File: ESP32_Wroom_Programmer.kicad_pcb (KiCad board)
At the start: 2 copper layers, 40.6 x 18 mm, 20 parts, among them J1 USB_C_Receptacle_USB2.0_16P, Q1 SS8050, Q2 SS8050, U1 Torex Semicon XC6206P332MR-G, U2 CH340C

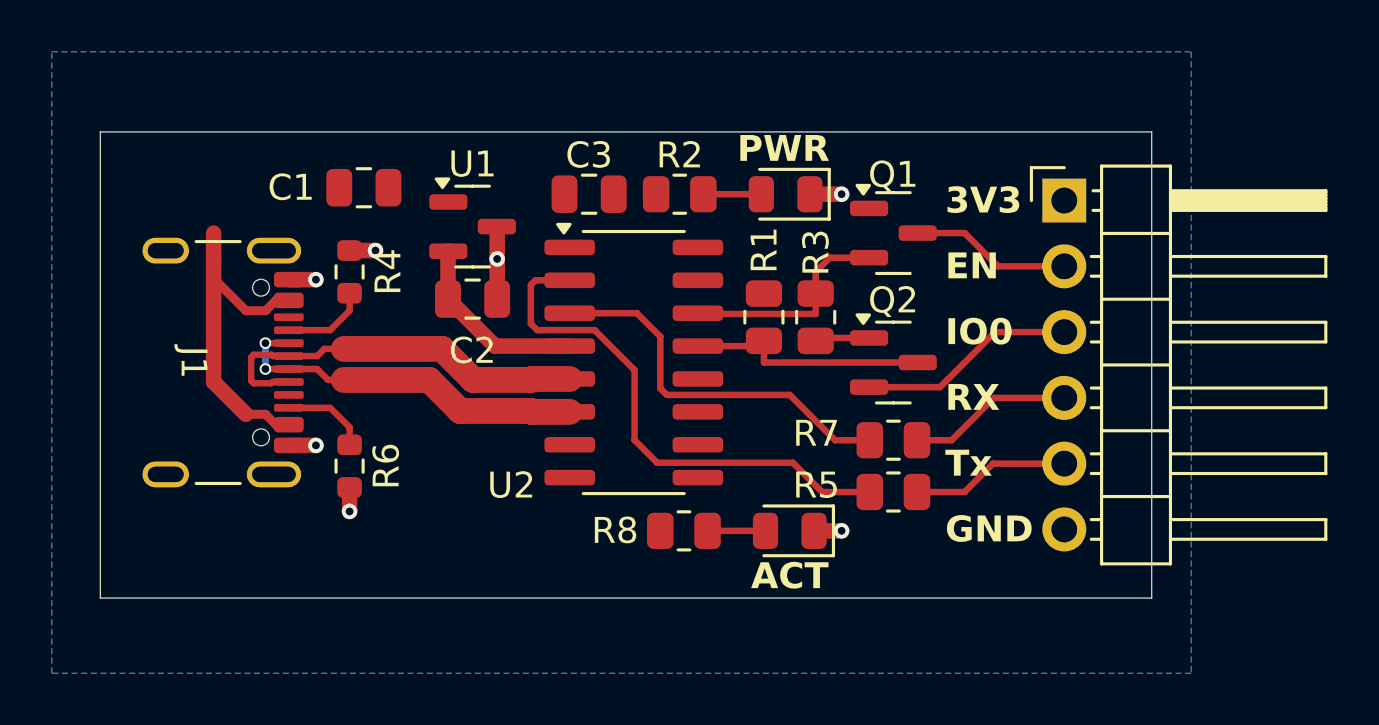
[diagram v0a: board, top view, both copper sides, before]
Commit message: fixed missing +3V3 connections
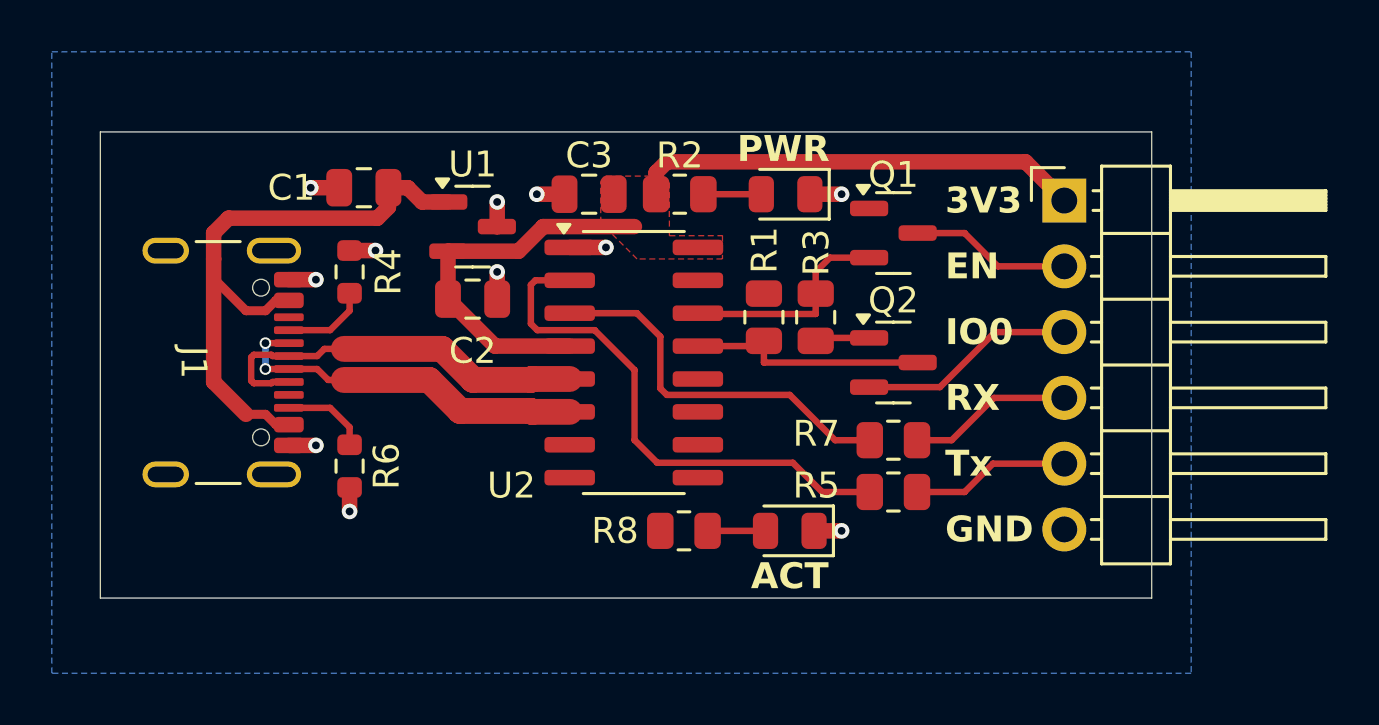
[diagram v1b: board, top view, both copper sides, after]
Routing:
- net +3V3: track 7.50 -> 32.5 mm
- net VBUS: track 13.7 -> 24.1 mm
- net GND: track 9.12 -> 11.7 mm, vias 7 -> 11
- added copper zone on F.Cu, net +3V3
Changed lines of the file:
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@@
 		(tags "capacitor")
 		(property "Reference" "C2"
-			(at 0 2.000001 360)
+			(at 0 2.000001 0)
 			(layer "F.SilkS")
 			(effects
@@
 		)
 		(property "Value" "1u"
-			(at 0 1.679999 360)
+			(at 0 1.679999 0)
 			(layer "F.Fab")
 			(effects
@@
 		)
 		(fp_text user "${REFERENCE}"
-			(at 0 0 360)
+			(at 0 0 0)
 			(layer "F.Fab")
 			(effects
@@
 		(tags "SOT TO_SOT_SMD")
 		(property "Reference" "U1"
-			(at 0 -2.4 360)
+			(at 0 -2.4 0)
 			(layer "F.SilkS")
 			(effects
@@
 		)
 		(property "Value" "Torex Semicon XC6206P332MR-G"
-			(at 0 2.4 360)
+			(at 0 2.4 0)
 			(layer "F.Fab")
 			(effects
@@
 		)
 		(fp_text user "${REFERENCE}"
-			(at 0 0 360)
+			(at 0 0 0)
 			(layer "F.Fab")
 			(effects
@@
 		(tags "capacitor")
 		(property "Reference" "C1"
-			(at 2.800001 0 360)
+			(at 2.800001 0 0)
 			(layer "F.SilkS")
 			(effects
@@
 		)
 		(property "Value" "1u"
-			(at 0 1.679999 360)
+			(at 0 1.679999 0)
 			(layer "F.Fab")
 			(effects
@@
 		)
 		(fp_text user "${REFERENCE}"
-			(at 0 0 360)
+			(at 0 0 0)
 			(layer "F.Fab")
 			(effects
@@
 	)
 	(segment
-		(start 142.199999 96)
-		(end 142.199999 94.762498)
+		(start 136.5 95.675)
+		(end 137.5 95.675)
 		(width 0.6)
 		(layer "F.Cu")
@@
 	)
 	(segment
-		(start 136.5 95.675)
-		(end 137.5 95.675)
+		(start 142.2 97.549999)
+		(end 142.199999 97.55)
 		(width 0.6)
 		(layer "F.Cu")
@@
 	)
 	(segment
-		(start 136.5 104.85)
-		(end 136.475 104.825)
+		(start 145 95.555)
+		(end 146.4 95.555)
+		(width 0.6)
+		(layer "F.Cu")
+		(net 1)
+	)
+	(segment
+		(start 142.2 94.737501)
+		(end 142.187501 94.75)
 		(width 0.6)
 		(layer "F.Cu")
@@
 	)
 	(segment
-		(start 142.199999 97.55)
-		(end 142.199999 96)
+		(start 143.731249 93.5)
+		(end 144.66875 93.5)
+		(width 0.6)
+		(layer "F.Cu")
+		(net 1)
+	)
+	(segment
+		(start 135.999999 93.25)
+		(end 135.000001 93.25)
+		(width 0.6)
+		(layer "F.Cu")
+		(net 1)
+	)
+	(segment
+		(start 142.2 96.5)
+		(end 142.2 97.549999)
+		(width 0.6)
+		(layer "F.Cu")
+		(net 1)
+	)
+	(segment
+		(start 136.5 104.85)
+		(end 136.475 104.825)
 		(width 0.6)
 		(layer "F.Cu")
@@
 		(net 1)
 	)
+	(segment
+		(start 142.2 93.8)
+		(end 142.2 94.737501)
+		(width 0.6)
+		(layer "F.Cu")
+		(net 1)
+	)
 	(via
 		(at 137.5 95.675)
@@
 	)
 	(via
+		(at 135.000001 93.25)
+		(size 0.6)
+		(drill 0.3)
+		(layers "F.Cu" "B.Cu")
+		(free yes)
+		(net 1)
+	)
+	(via
+		(at 143.731249 93.5)
+		(size 0.6)
+		(drill 0.3)
+		(layers "F.Cu" "B.Cu")
+		(free yes)
+		(net 1)
+	)
+	(via
 		(at 155.5 93.5)
 		(size 0.6)
@@
 	)
 	(via
+		(at 142.2 93.8)
+		(size 0.6)
+		(drill 0.3)
+		(layers "F.Cu" "B.Cu")
+		(free yes)
+		(net 1)
+	)
+	(via
 		(at 135.2 96.8)
 		(size 0.6)
@@
 	)
 	(via
-		(at 142.199999 96)
+		(at 146.4 95.555)
 		(size 0.6)
 		(drill 0.3)
 		(layers "F.Cu" "B.Cu")
+		(free yes)
+		(net 1)
+	)
+	(via
+		(at 142.2 96.5)
+		(size 0.6)
+		(drill 0.3)
+		(layers "F.Cu" "B.Cu")
+		(free yes)
 		(net 1)
 	)
@@
 	)
 	(segment
+		(start 131.25 95)
+		(end 131.825 94.425)
+		(width 0.6)
+		(layer "F.Cu")
+		(net 3)
+	)
+	(segment
+		(start 140.3125 93.8)
+		(end 139.3 93.8)
+		(width 0.6)
+		(layer "F.Cu")
+		(net 3)
+	)
+	(segment
 		(start 133.656317 102.4)
 		(end 133.256317 102)
@@
 	)
 	(segment
+		(start 138 94)
+		(end 138 93.25)
+		(width 0.6)
+		(layer "F.Cu")
+		(net 3)
+	)
+	(segment
 		(start 133.656317 97.6)
 		(end 133.256317 98)
@@
 	)
 	(segment
+		(start 139.3 93.8)
+		(end 138.75 93.25)
+		(width 0.6)
+		(layer "F.Cu")
+		(net 3)
+	)
+	(segment
 		(start 132.5 98)
 		(end 131.25 96.75)
@@
 	)
 	(segment
+		(start 138.75 93.25)
+		(end 138 93.25)
+		(width 0.6)
+		(layer "F.Cu")
+		(net 3)
+	)
+	(segment
 		(start 133.256317 98)
 		(end 132.5 98)
@@
 	)
 	(segment
-		(start 131.25 95)
-		(end 131.25 96)
+		(start 137.575 94.425)
+		(end 138 94)
+		(width 0.6)
+		(layer "F.Cu")
+		(net 3)
+	)
+	(segment
+		(start 131.25 96)
+		(end 131.25 95)
 		(width 0.6)
 		(layer "F.Cu")
@@
 	)
 	(segment
+		(start 131.825 94.425)
+		(end 137.575 94.425)
+		(width 0.6)
+		(layer "F.Cu")
+		(net 3)
+	)
+	(segment
 		(start 134.155 102.4)
 		(end 133.656317 102.4)
@@
 	)
 	(segment
+		(start 140.3125 95.7)
+		(end 143.027316 95.7)
+		(width 0.6)
+		(layer "F.Cu")
+		(net 4)
+	)
+	(segment
+		(start 148.75 92.25)
+		(end 148.3375 92.6625)
+		(width 0.6)
+		(layer "F.Cu")
+		(net 4)
+	)
+	(segment
 		(start 148.262499 93.575001)
 		(end 148.3375 93.5)
@@
 	)
 	(segment
+		(start 148.3375 92.6625)
+		(end 148.3375 93.5)
+		(width 0.6)
+		(layer "F.Cu")
+		(net 4)
+	)
+	(segment
 		(start 148.3375 93.5)
 		(end 148.425 93.5)
@@
 	)
 	(segment
+		(start 164.1 93.745)
+		(end 162.605 92.25)
+		(width 0.6)
+		(layer "F.Cu")
+		(net 4)
+	)
+	(segment
+		(start 162.605 92.25)
+		(end 148.75 92.25)
+		(width 0.6)
+		(layer "F.Cu")
+		(net 4)
+	)
+	(segment
+		(start 143.977316 94.75)
+		(end 147.5 94.75)
+		(width 0.6)
+		(layer "F.Cu")
+		(net 4)
+	)
+	(segment
+		(start 143.027316 95.7)
+		(end 143.977316 94.75)
+		(width 0.6)
+		(layer "F.Cu")
+		(net 4)
+	)
+	(segment
 		(start 140.300001 95.712499)
 		(end 140.3125 95.7)
@@
 	)
 	(zone
+		(net 4)
+		(net_name "+3V3")
+		(layer "F.Cu")
+		(hatch edge 0.5)
+		(priority 100)
+		(connect_pads yes
+			(clearance 0.2)
+		)
+		(min_thickness 0.2)
+		(filled_areas_thickness no)
+		(fill yes
+			(thermal_gap 0.2)
+			(thermal_bridge_width 0.5)
+		)
+		(polygon
+			(pts
+				(xy 146.2 93) (xy 146.4 92.8) (xy 148.6 92.8) (xy 148.847617 93.048547) (xy 148.847617 94.148547)
+				(xy 148.850514 95.103114) (xy 150.9 95.1) (xy 150.9 96) (xy 147.6 96) (xy 146.2 94.6)
+			)
+		)
+	)
+	(zone

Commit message: there were still some connections missing...
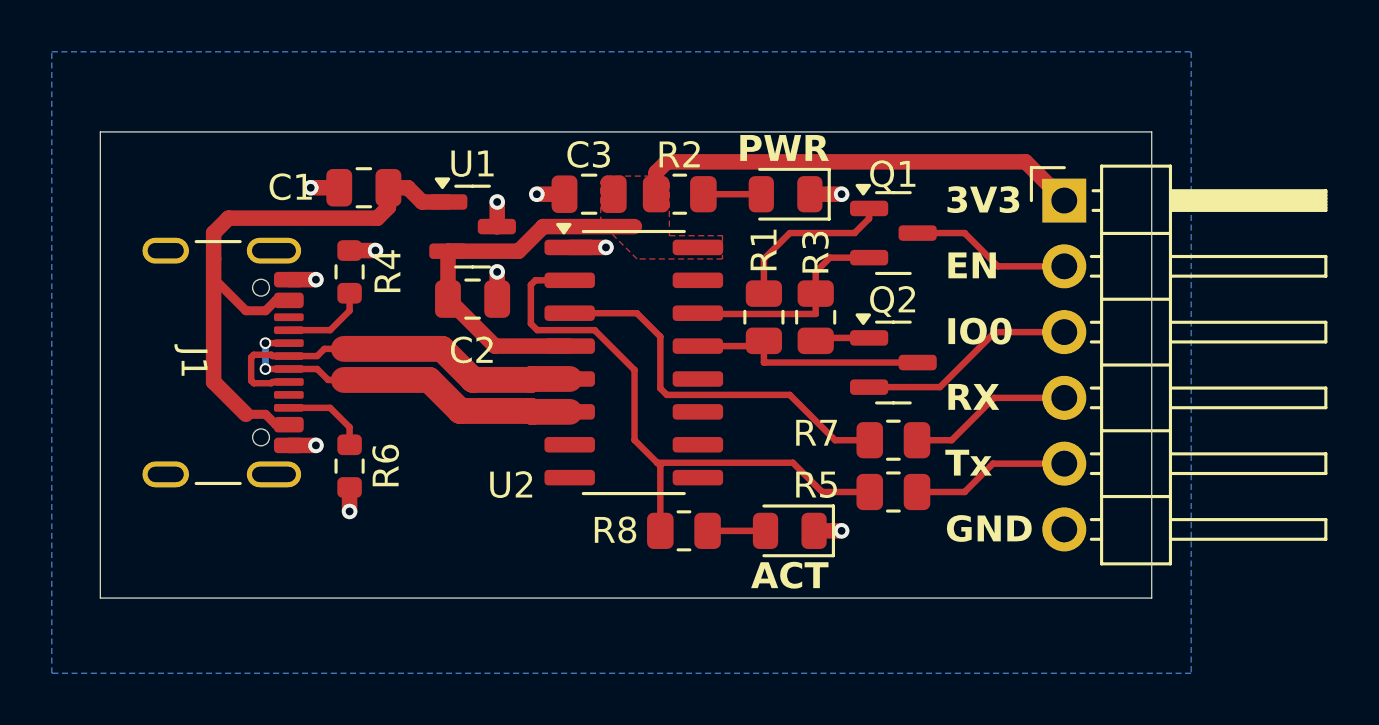
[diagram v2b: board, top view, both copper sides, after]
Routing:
- net Net-(Q1-B): track 0.00 -> 6.43 mm
- net /Conv_Tx: track 20.6 -> 23.2 mm
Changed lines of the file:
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@@
+	)
+	(segment
+		(start 152.5 96)
+		(end 153.5 95)
+		(width 0.25)
+		(layer "F.Cu")
+		(net 20)
+	)
+	(segment
+		(start 156 95)
+		(end 156.5625 94.4375)
+		(width 0.25)
+		(layer "F.Cu")
+		(net 20)
+	)
+	(segment
+		(start 152.5 97.3375)
+		(end 152.5 96)
+		(width 0.25)
+		(layer "F.Cu")
+		(net 20)
+	)
+	(segment
+		(start 156.5625 94.4375)
+		(end 156.5625 94.05)
+		(width 0.25)
+		(layer "F.Cu")
+		(net 20)
+	)
+	(segment
+		(start 153.5 95)
+		(end 156 95)
+		(width 0.25)
+		(layer "F.Cu")
+		(net 20)
 	)
 	(segment
@@
 	)
 	(segment
+		(start 148.5 106.5)
+		(end 148.5 103.99)
+		(width 0.25)
+		(layer "F.Cu")
+		(net 24)
+	)
+	(segment
 		(start 143.5 97)
 		(end 143.5 98.5)
@@
 		(end 148.38 103.87)
 		(width 0.25)
+		(layer "F.Cu")
+		(net 24)
+	)
+	(segment
+		(start 148.5 103.99)
+		(end 148.38 103.87)
+		(width 0.25)

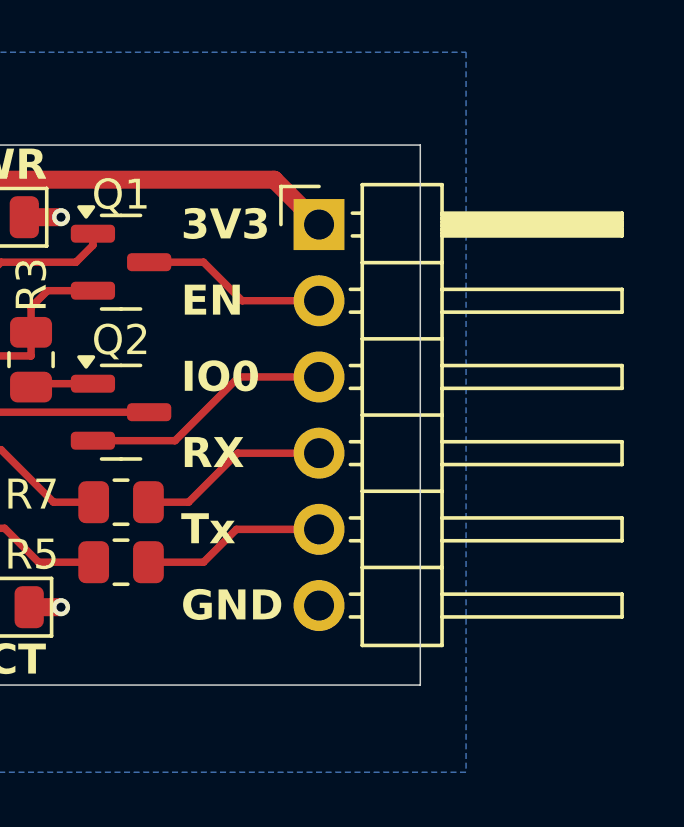
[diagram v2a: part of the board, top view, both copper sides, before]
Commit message: added ground to USB-C Shield
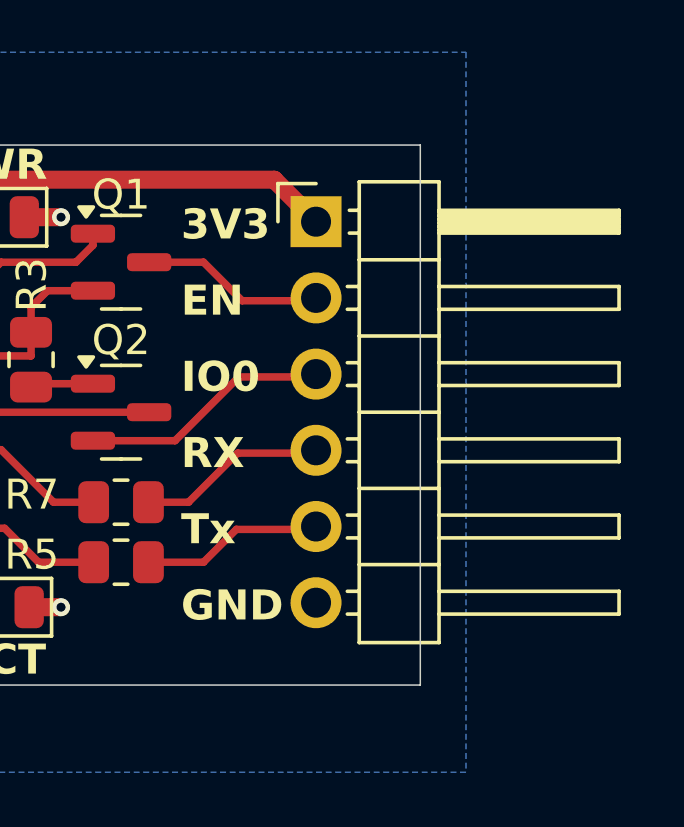
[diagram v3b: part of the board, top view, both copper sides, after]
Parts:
- removed PROG1: Conn_01x06, Connector_PinHeader_2.54mm:PinHeader_1x06_P2.54mm_Horizontal
- added J2: Conn_01x06, Connector_PinHeader_2.54mm:PinHeader_1x06_P2.54mm_Horizontal, F.Cu at (164.0, 93.7)
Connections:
- J1 pad S1: unconnected-(J1-SHIELD-PadS1) -> GND
